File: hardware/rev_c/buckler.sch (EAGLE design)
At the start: 62 parts, among them J1 NRF52832DK_SHIELD, J12 GROVE-CONNECTOR-DIP(4P-2.0), J13 GROVE-CONNECTOR-DIP(4P-2.0), J14 GROVE-CONNECTOR-DIP(4P-2.0), J15 GROVE-CONNECTOR-DIP(4P-2.0), J16 DB25_5747846, J17 DM3AT-SF-PEJM5, J18 NHD-0216KZWSERIAL, J7 M10", U1 ADXL327, U2 MAX44009, U4 MS5637-02BA03, U5 SI7021-A20-GM1, U6 SIP32510, U7 LSM9DS1TR

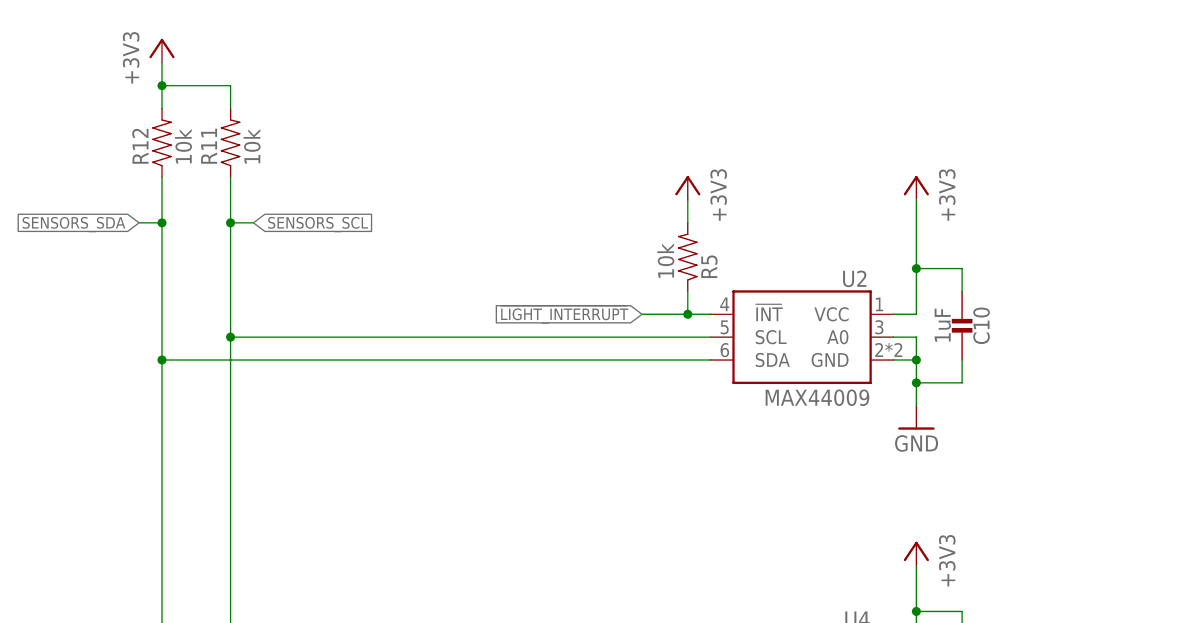
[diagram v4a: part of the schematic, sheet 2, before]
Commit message: add OPT light sensor
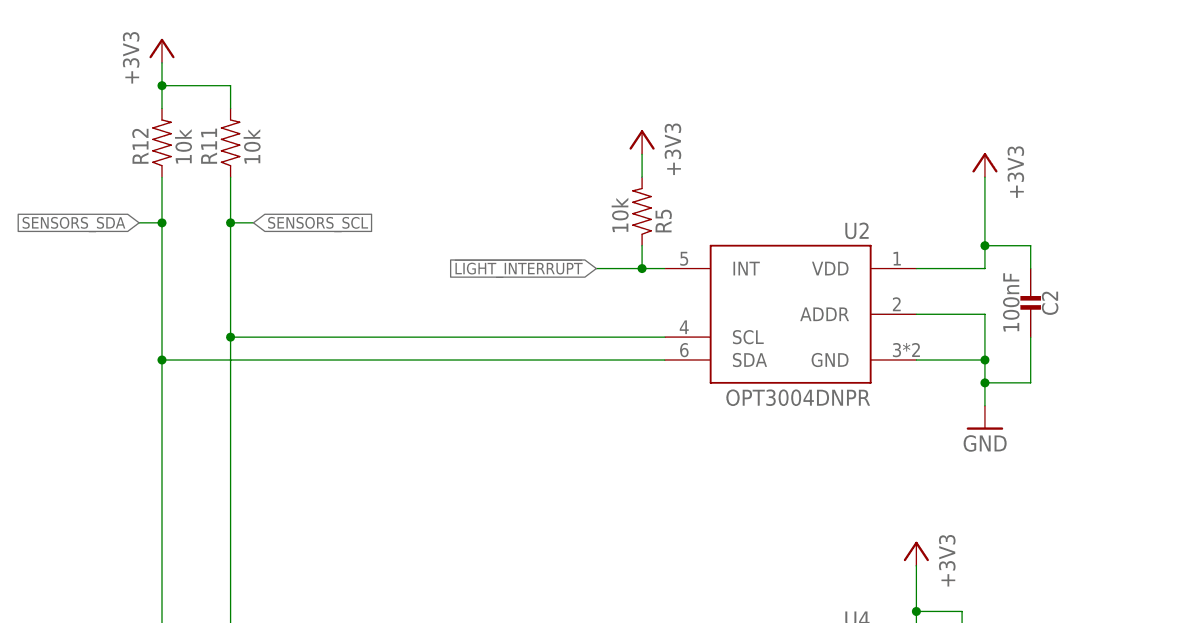
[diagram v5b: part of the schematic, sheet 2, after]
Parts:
- removed C10: 1uF, passives:CAPACITOR0402_CAP
- added C2: 100nF, passives:CAPACITOR0402_CAP
- U2: value MAX44009 -> OPT3004DNPR; device chips:MAX44009 -> chips:OPT3004DNPR; DESCRIPTION SENSOR AMBIENT LIGHT 6UTDFN -> (none); MANUFACTURER Maxim Integrated -> (none)
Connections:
- net !LIGHT_INTERRUPT: now also U2.INT; no longer U2.!INT
- net +3V3: now also C2.1, U2.VDD; no longer C10.1, U2.VCC
- net GND: now also C2.2, U2.ADDR; no longer C10.2, U2.A0
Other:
- note added: "I2C Address: 0x44"
- note removed: "I2C Address: 0x4A"
- moved on the sheet: R5

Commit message: zip it up for quote
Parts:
- removed C14: 10nF, passives:CAPACITOR0402_CAP
- removed R15: 100k, passives:RESISTOR0402_RES
- removed U7: LSM9DS1TR, chips:LSM9DS1TR
- added C10: 100nF, passives:CAPACITOR0402_CAP
- added R6: 10k, passives:RESISTOR0402_RES
- added U3: MS5637-02BA03, chips:MS5637-02BA03
- C11: value 4.7uF -> 100nF; DESCRIPTION CAP CER 4.7UF 10V X5R 0402 -> CAP CER 0.1UF 16V X7R 0402; DIGIKEY 1276-1480-1-ND -> 490-4759-1-ND; MANUFACTURER Samsung Electro-Mechanics -> Murata; MPN CL05A475KP5NRNC -> GCM155R71C104KA55D
- C13: value 100nF -> 4.7uF; DESCRIPTION CAP CER 0.1UF 16V X7R 0402 -> CAP CER 4.7UF 10V X5R 0402; DIGIKEY 490-4759-1-ND -> 1276-1480-1-ND; MANUFACTURER Murata -> Samsung Electro-Mechanics; MPN GCM155R71C104KA55D -> CL05A475KP5NRNC
- C2: value 100nF -> 10nF; DESCRIPTION CAP CER 0.1UF 16V X7R 0402 -> CAP CER 10000PF 25V X7R 0402; DIGIKEY 490-4759-1-ND -> 399-1279-1-ND; MANUFACTURER Murata -> KEMET; MPN GCM155R71C104KA55D -> C0402C103J3RACTU
- D3: value YELLOW -> GREEN; DESCRIPTION LED YELLOW CLEAR CHIP SMD -> LED GREEN CLEAR CHIP SMD; DIGIKEY 160-1437-1-ND -> 160-1435-1-ND; MPN LTST-C190KSKT -> LTST-C190KGKT
- D5: value GREEN -> YELLOW; DESCRIPTION LED GREEN CLEAR CHIP SMD -> LED YELLOW CLEAR CHIP SMD; DIGIKEY 160-1435-1-ND -> 160-1437-1-ND; MPN LTST-C190KGKT -> LTST-C190KSKT
- J10: device SparkFun-Connectors:M081X08 -> SparkFun-Connectors:M06SIP; DIGIKEY S1011EC-08-ND -> S1011EC-06-ND
- J9: device SparkFun-Connectors:M06SIP -> SparkFun-Connectors:M081X08; DIGIKEY S1011EC-06-ND -> S1011EC-08-ND
- R13: value 10k -> 100k; DESCRIPTION RES SMD 10K OHM 1% 1/16W 0402 -> RES SMD 100K OHM 1% 1/5W 0402; DIGIKEY 1276-3431-1-ND -> 541-100KYCT-ND; MANUFACTURER Samsung Electro-Mechanics -> Vishay Dale; MPN RC1005F103CS -> CRCW0402100KFKEDHP
- U2: value OPT3004DNPR -> LSM9DS1TR; device chips:OPT3004DNPR -> chips:LSM9DS1TR
- U4: value MS5637-02BA03 -> OPT3004DNPR; device chips:MS5637-02BA03 -> chips:OPT3004DNPR; DESCRIPTION SENSOR 17.4PSIA I2C 24B 4-QFN -> (none)
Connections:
- net !BUTTON_0: now also J10.4, R12.1; no longer J9.4, R13.1
- net !IMU_INTERRUPT: now also U2.INT1_A/G; no longer U7.INT1_A/G
- net !LCD_CS: now also J9.8; no longer J10.8
- net !LED_1: now also D5.CATHODE; no longer D3.CATHODE
- net !LIGHT_INTERRUPT: now also U4.INT; no longer U2.INT
- net !RESET: now also R9.1; no longer R10.1
- net !SD_CS: now also J9.4, R7.1; no longer J10.4, R8.1
- net !SD_DETECT: now also R13.1; no longer R14.1
- net +3V3: now also C10.2, C11.2, C12.1, R14.2, R9.2, U2.CS_A/G, U2.CS_M, U2.VDDIO, U3.VDD; no longer C12.2, C13.2, C2.1, R13.2, R15.2, U7.CS_A/G, U7.CS_M, U7.VDD, U7.VDDIO
- net ANALOG_ACCEL_X: now also J10.3; no longer J9.3
- net ANALOG_ACCEL_Y: now also J10.2; no longer J9.2
- net ANALOG_ACCEL_Z: now also J10.1; no longer J9.1
- net GND: now also C10.1, C11.1, C12.2, C13.2, C2.1, D3.CATHODE, U2.SDO_A/G, U2.SDO_M, U3.GND, U4.ADDR; no longer C11.2, C12.1, C13.1, C14.1, C2.2, D5.CATHODE, U2.ADDR, U7.GND, U7.SDO_A/G, U7.SDO_M
- net GROVE_A0: now also J10.5; no longer J9.5
- net GROVE_A1: now also J10.6; no longer J9.6
- net LCD_MISO: now also J9.6; no longer J10.6
- net LCD_MOSI: now also J9.5; no longer J10.5
- net LCD_SCLK: now also J9.7; no longer J10.7
- net N$1: now also U2.C1; no longer U7.C1
- net N$18: now also C13.1, R13.2, R6.2; no longer C11.1, R14.2, R9.2
- net N$3: now also D3.ANODE; no longer D5.ANODE
- net N$5: now also D5.ANODE; no longer D3.ANODE
- net N$6: now also C2.2, U2.CAP; no longer C14.2, U7.CAP
- net SD_ENABLE: now also R14.1; no longer R15.1
- net SD_MISO: now also J9.2, R8.1; no longer J10.2, R9.1
- net SD_MOSI: now also J9.1, R6.1; no longer J10.1, R7.1
- net SD_SCLK: now also J9.3; no longer J10.3
- net SENSORS_SCL: now also R10.1, U2.SCL/SPC, U3.SCL; no longer R11.1, U2.SCL, U7.SCL/SPC
- net SENSORS_SDA: now also R11.1, U2.SDA/SDI/SDO, U3.SDA; no longer R12.1, U2.SDA, U7.SDA/SDI/SDO
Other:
- moved on the sheet: C12, C2, D3, D5, R11, R13, R14, R7, R8
